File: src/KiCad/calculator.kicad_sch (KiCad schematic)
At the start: 30 parts, among them J1 USB_C_Receptacle_USB2.0_14P, SW1 1, SW10 0, SW11 ., SW12 x10, SW13 DEL, SW14 x, SW15 +, SW16 Ans, SW17 AC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

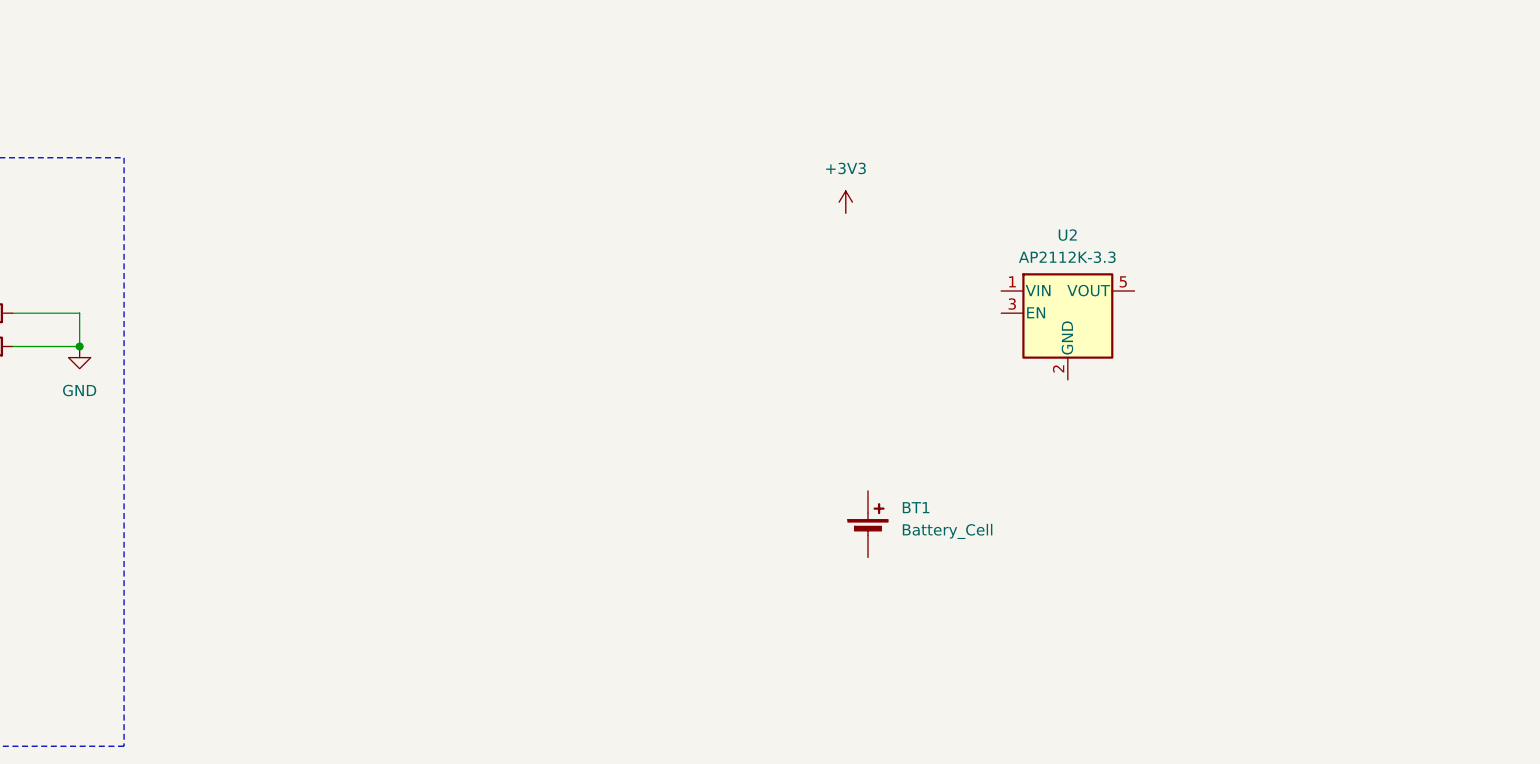
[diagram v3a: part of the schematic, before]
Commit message: Add battery charger and update symbols
Add MCP73831 battery charger symbol and instance (U3) and annotate the battery charging area; convert/update several component symbol definitions (resistor -> capacitor template, switch/pushbutton symbol) and reorganize MCU/resistor symbol entries. Replace AP2112K regulator symbol with power:GND instance (#PWR05) and adjust related properties and footprints. Add numerous wires, junctions, labels (e.g. "Battery charging", "VRAW", "charging_stat 5V!!") and update schematic net connections. Update project used_designators in calculator.kicad_pro to reflect added/renamed components.
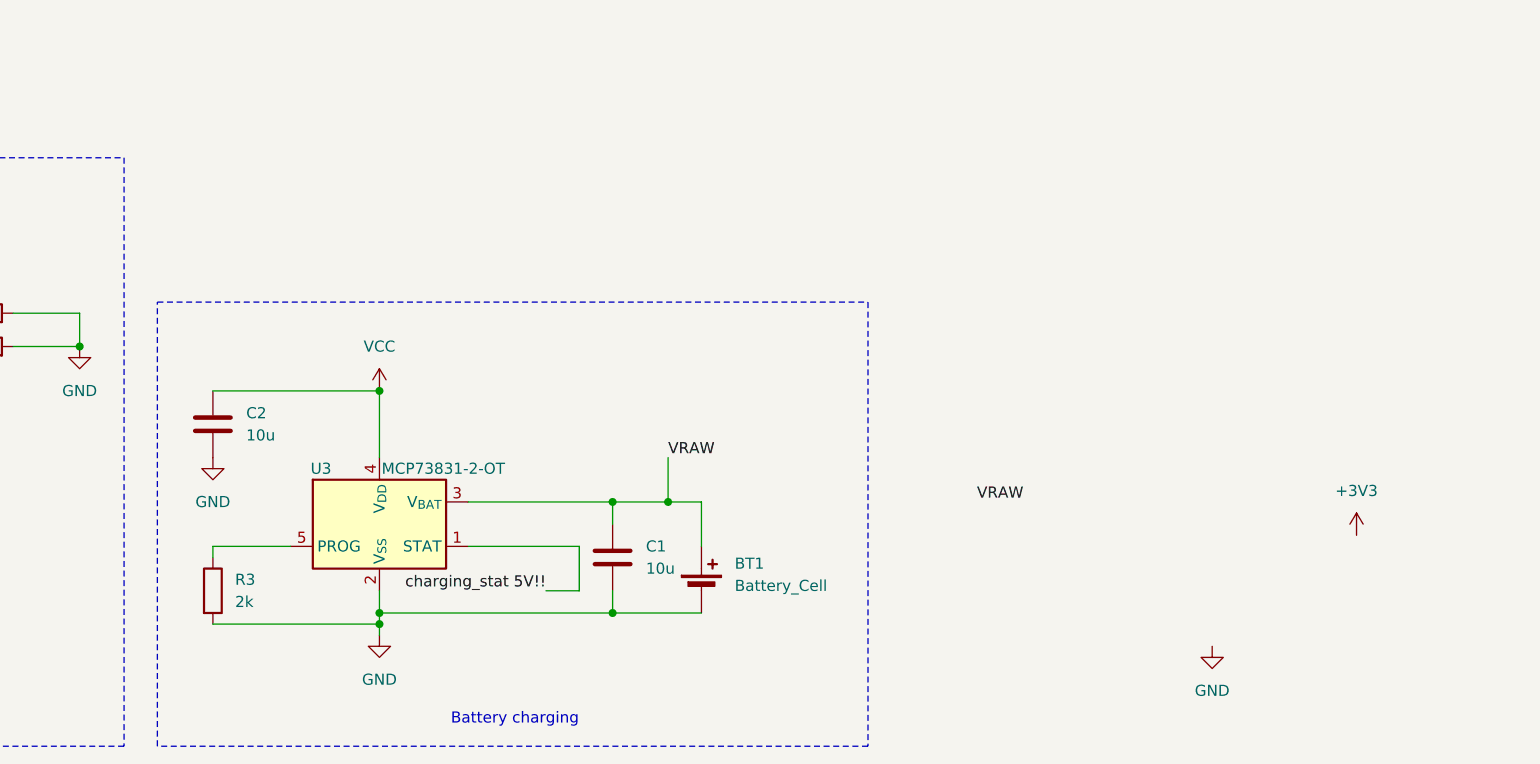
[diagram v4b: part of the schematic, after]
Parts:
- removed U2: AP2112K-3.3, Package_TO_SOT_SMD:SOT-23-5, symbol Regulator_Linear:AP2112K-3.3
- added C1, C2: 10u, symbol Device:C
- added R3: 2k, symbol Device:R
- added U3: MCP73831-2-OT, Package_TO_SOT_SMD:SOT-23-5, symbol Battery_Management:MCP73831-2-OT
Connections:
- net GND: now also BT1.2 (-), C1.1, C2.1, R3.2, U3.2 (V_{SS})
- net VCC: now also C2.2, U3.4 (V_{DD})
- net VRAW: now reaches BT1.1 (+)
- net VRAW: now also C1.2, U3.3 (V_{BAT})
- new net: R3.1, U3.5 (PROG)
- new net charging_stat 5V!!: U3.1 (STAT)
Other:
- note added: "Battery charging"
- moved on the sheet: BT1

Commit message: voltage regulation done
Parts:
- added U2: XC6210B332MR, Package_TO_SOT_SMD:SOT-23-5, symbol Regulator_Linear:XC6210B332MR
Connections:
- net +3V3: now also U2.5 (VOUT)
- net GND: now also U2.2 (GND)
- net VRAW: now also U2.1 (VIN)
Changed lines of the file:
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@@
 	(wire
 		(pts
+			(xy 190.5 252.73) (xy 199.39 252.73)
+		)
+		(stroke
+			(width 0)
+			(type default)
+		)
+	)
+	(wire
+		(pts
 			(xy 311.15 228.6) (xy 311.15 231.14)
 		)
@@
 	(wire
 		(pts
+			(xy 212.09 265.43) (xy 212.09 269.24)
+		)
+		(stroke
+			(width 0)
+			(type default)
+		)
+	)
+	(wire
+		(pts
 			(xy 321.31 228.6) (xy 322.58 228.6)
 		)
@@
 	(wire
 		(pts
+			(xy 224.79 252.73) (xy 228.6 252.73)
+		)
+		(stroke
+			(width 0)
+			(type default)
+		)
+	)
+	(wire
+		(pts
 			(xy 43.18 264.16) (xy 43.18 266.7)
 		)
@@
 	)
 	(symbol
+		(lib_id "Regulator_Linear:XC6210B332MR")
+		(at 212.09 255.27 0)
+		(unit 1)
+		(body_style 1)
+		(exclude_from_sim no)
+		(in_bom yes)
+		(on_board yes)
+		(in_pos_files yes)
+		(dnp no)
+		(fields_autoplaced yes)
+		(property "Reference" "U2"
+			(at 212.09 245.11 0)
+			(show_name no)
+			(do_not_autoplace no)
+			(effects
+				(font
+					(size 1.27 1.27)
+				)
+			)
+		)
+		(property "Value" "XC6210B332MR"
+			(at 212.09 247.65 0)
+			(show_name no)
+			(do_not_autoplace no)
+			(effects
+				(font
+					(size 1.27 1.27)
+				)
+			)
+		)
+		(property "Footprint" "Package_TO_SOT_SMD:SOT-23-5"
+			(at 212.09 255.27 0)
+			(hide yes)
+			(show_name no)
+			(do_not_autoplace no)
+			(effects
+				(font
+					(size 1.27 1.27)
+				)
+			)
+		)
+		(property "Datasheet" "https://www.torexsemi.com/file/xc6210/XC6210.pdf"
+			(at 231.14 280.67 0)
+			(hide yes)
+			(show_name no)
+			(do_not_autoplace no)
+			(effects
+				(font
+					(size 1.27 1.27)
+				)
+			)
+		)
+		(property "Description" "700mA, Low Drop-out Voltage Regulator, Fixed Output 3.3V, SOT-23-5"
+			(at 212.09 255.27 0)
+			(hide yes)
+			(show_name no)
+			(do_not_autoplace no)
+			(effects
+				(font
+					(size 1.27 1.27)
+				)
+			)
+		)
+		(pin "1"
+		)
+		(pin "5"
+		)
+		(pin "2"
+		)
+		(pin "4"
+		)
+		(pin "3"
+		)
+		(instances
+			(project "calculator"
+				(path "/8a314358-54d1-4700-9196-0b053571b484"
+					(reference "U2")
+					(unit 1)
+				)
+			)
+		)
+	)
+	(symbol
 		(lib_id "Switch:SW_Push")
 		(at 349.25 209.55 0)
@@
 	(symbol
 		(lib_id "power:+3V3")
-		(at 228.6 256.54 0)
+		(at 228.6 252.73 0)
 		(unit 1)
 		(body_style 1)
@@
 		(fields_autoplaced yes)
 		(property "Reference" "#PWR08"
-			(at 228.6 260.35 0)
+			(at 228.6 256.54 0)
 			(hide yes)
 			(show_name no)
@@
 		)
 		(property "Value" "+3V3"
-			(at 228.6 251.46 0)
+			(at 228.6 247.65 0)
 			(show_name no)
 			(do_not_autoplace no)
@@
 		)
 		(property "Footprint" ""
-			(at 228.6 256.54 0)
+			(at 228.6 252.73 0)
 			(hide yes)
 			(show_name no)
@@
 		)
 		(property "Datasheet" ""
-			(at 228.6 256.54 0)
+			(at 228.6 252.73 0)
 			(hide yes)
 			(show_name no)
@@
 		)
 		(property "Description" "Power symbol creates a global label with name \"+3V3\""
-			(at 228.6 256.54 0)
+			(at 228.6 252.73 0)
 			(hide yes)
 			(show_name no)

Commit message: forgot to save
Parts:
- added C3: 1u, symbol Device:C
- added C4: 22u, symbol Device:C
- added D1: 1N914, Diode_THT:D_DO-35_SOD27_P7.62mm_Horizontal, symbol Diode:1N914
- added R4: 100k, symbol Device:R
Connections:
- net +3V3: now also C4.1
- net GND: now also C3.2, C4.2, R4.2
- net VRAW: now also SW22.1, C3.1
- net EN_reg: now reaches SW22.2
- net EN_reg: now also U2.3 (CE), D1.1 (K), R4.1
- net at U1.6 (GPIO1): now also D1.2 (A)
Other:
- note added: "Voltage regulation"
- moved on the sheet: SW22, U2

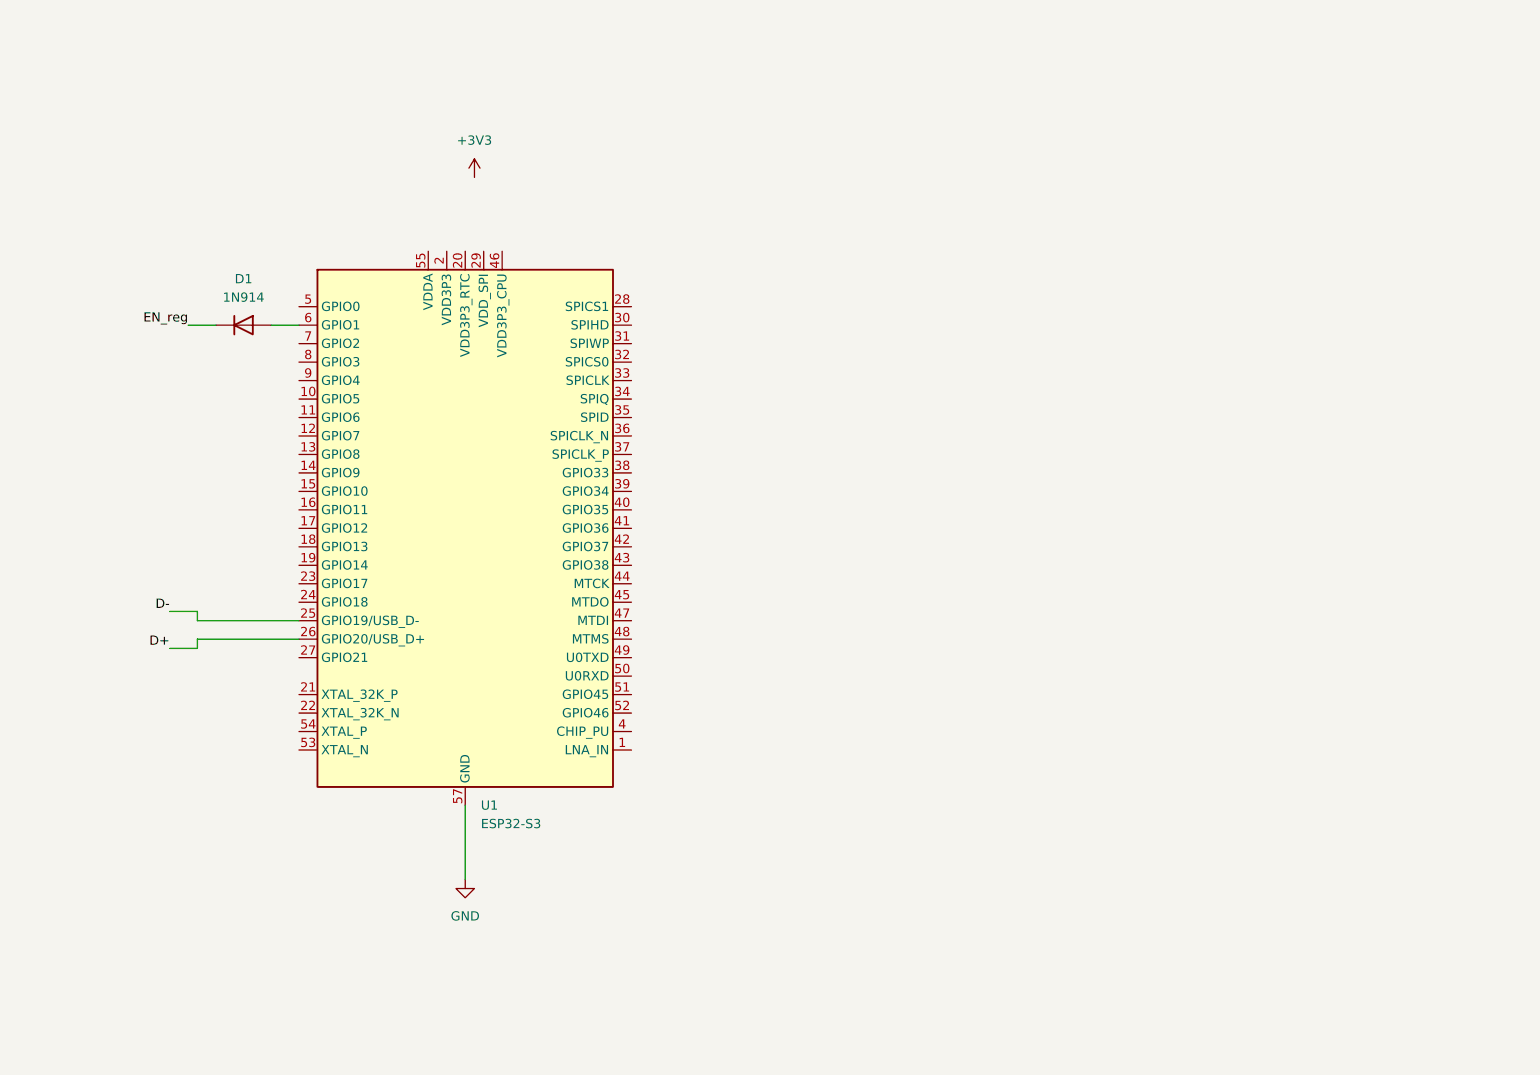
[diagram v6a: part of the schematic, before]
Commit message: XTAL N and P wired
wired the external crystal for clock
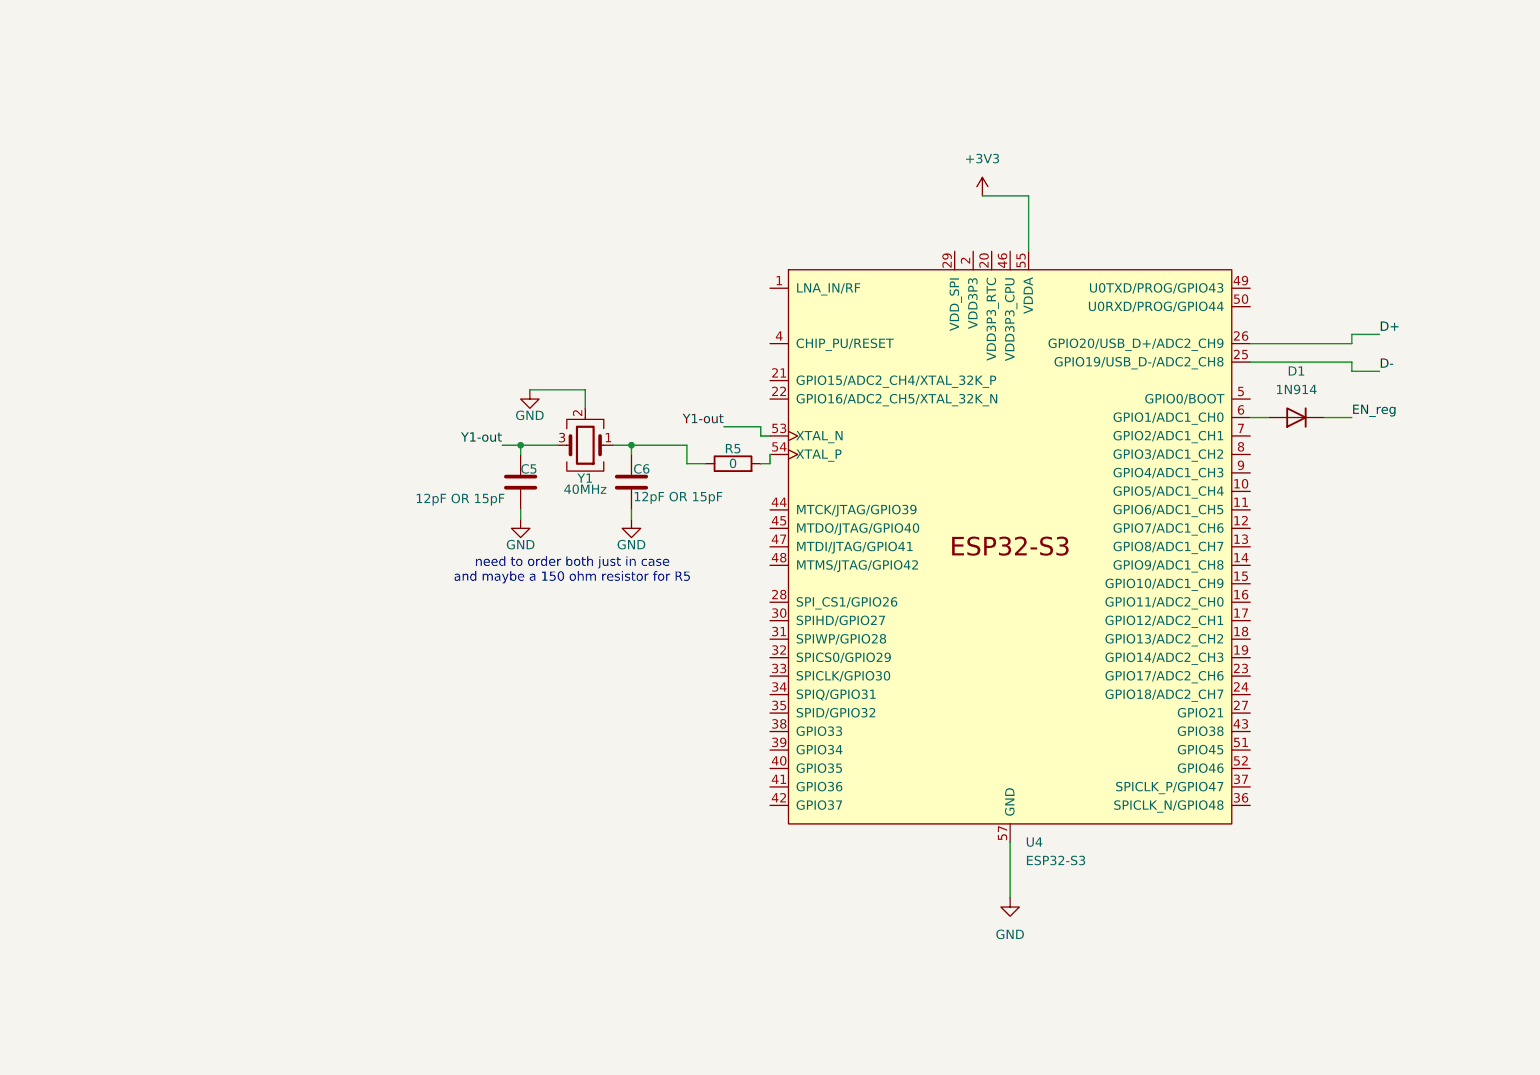
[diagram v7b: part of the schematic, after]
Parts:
- removed U1: ESP32-S3, Package_DFN_QFN:QFN-56-1EP_7x7mm_P0.4mm_EP4x4mm, symbol MCU_Espressif:ESP32-S3
- added C5, C6: 12pF OR 15pF, symbol Device:C
- added R5: 0, symbol Device:R
- added U4: ESP32-S3, Package_DFN_QFN:QFN-56-1EP_7x7mm_P0.4mm_EP5.6x5.6mm, symbol symbols:ESP32-S3
- added Y1: 40MHz, symbol Device:Crystal_GND24
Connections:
- net +3V3: now also U4.55 (VDDA), U4.56 (VDDA)
- net D+: now also U4.26 (GPIO20/USB_D+/ADC2_CH9)
- net D-: now also U4.25 (GPIO19/USB_D-/ADC2_CH8)
- net GND: now also C5.2, C6.2, U4.57 (GND), Y1.2 (G), Y1.4 (G)
- net at D1.2 (A): now also U4.6 (GPIO1/ADC1_CH0)
- new net: C6.1, R5.1, Y1.1
- new net: R5.2, U4.54 (XTAL_P)
- new net VDD3P3: U4.2 (VDD3P3), U4.3 (VDD3P3)
- new net Y1-out: C5.1, U4.53 (XTAL_N), Y1.3
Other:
- note added: "need to order both just in case and maybe a 150 ohm resistor for R5"
- moved on the sheet: D1

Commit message: Analog power
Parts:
- added C10: 1uF, symbol Device:C
- added C11: 10uF, symbol Device:C
- added C7: 1u, symbol Device:C
- added C8, C9: 0.1uF, symbol Device:C
- added L1: 2.0nH, symbol Device:L
- C5, C6: type (none) -> C0G (NP0)
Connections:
- net +3V3: now also C10.1, C11.1, C7.1, C9.1, L1.1
- net GND: now also C10.2, C11.2, C7.2, C8.2, C9.2
- net VDD3P3: now also C8.1, L1.2
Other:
- note added: "VDDD3P3(2, 3)"
- note added: "need to order both just in case and maybe a 120 ohm resistor for R5"
- note removed: "need to order both just in case and maybe a 150 ohm resistor for R5"
